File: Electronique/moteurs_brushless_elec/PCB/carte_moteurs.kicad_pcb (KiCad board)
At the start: 2 copper layers, 154 x 65 mm, 86 parts, among them J1 CONN_SERIAL, J2 swdio, J3 FAN, K1 Maxon-200142, K2 Maxon-200142, P1 CONN_I2C, P2 CONN_FREE, P3 CONN_CAN, P4 encoder_2, P5 encoder_1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

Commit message: trous et dim o
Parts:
- C2, Cboot2, Cen2, Coff2, Cp2, Cpul2, D10, D6, R8, R9, Rdd2, Ren2, Roff2, Rp2, Rpul2, U5, U6: moved to B.Cu
- moved Y1 319.6 mm to (242.0, 144.0)
- moved C3 312.7 mm to (229.2, 145.2)
- moved C4 312.7 mm to (236.2, 156.2)
- moved R14 298.7 mm to (226.0, 154.0), turned to 0 degrees
- moved P1 268.7 mm to (176.0, 123.0)
- moved J2 268.7 mm to (174.0, 146.0), turned to 270 degrees
- moved JP1 260.3 mm to (176.1, 89.8)
- moved R5 241.9 mm to (162.2, 103.1)
- moved P3 241.0 mm to (176.0, 129.5), turned to 90 degrees
- moved U3 240.1 mm to (152.7, 159.8), turned to 270 degrees
- moved D5 239.5 mm to (161.0, 139.0)
- moved R6 238.4 mm to (159.0, 131.0), turned to 0 degrees
- moved J1 237.5 mm to (176.0, 134.0), turned to 270 degrees
- moved P2 237.2 mm to (176.0, 113.5)
- moved C5 237.1 mm to (152.0, 113.0), turned to 90 degrees
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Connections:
- J3 pad 1: VCC -> VDD
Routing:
- net GND: track 0.00 -> 222.6 mm, vias 0 -> 4
- net VDD: track 0.00 -> 53.3 mm, vias 0 -> 1
- net VCC: track 0.00 -> 49.8 mm, vias 0 -> 2
- net /motor_part/DIAG_2: track 0.00 -> 44.6 mm, vias 0 -> 2
- net Net-(K1-Pad5): track 0.00 -> 37.6 mm, vias 0 -> 1
- net Net-(K1-Pad1): track 0.00 -> 30.0 mm, vias 0 -> 1
- net Net-(F2-Pad2): track 0.00 -> 28.9 mm
- net Net-(F1-Pad2): track 0.00 -> 28.9 mm
- net Net-(K2-Pad1): track 0.00 -> 28.6 mm, vias 0 -> 1
- net Net-(K2-Pad9): track 0.00 -> 26.1 mm, vias 0 -> 1
- net Net-(K2-Pad5): track 0.00 -> 25.9 mm, vias 0 -> 1
- net Net-(K2-Pad3): track 0.00 -> 25.5 mm, vias 0 -> 1
- net Net-(Rsense2-Pad1): track 0.00 -> 24.3 mm
- net Net-(K1-Pad3): track 0.00 -> 21.9 mm, vias 0 -> 1
- net /motor_part/Vref2: track 0.00 -> 20.6 mm, vias 0 -> 2
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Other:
- net class Default: trace_width 0.508 -> 0.4

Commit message: trous et dim
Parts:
- C1, C5, Cboot1, Cen1, Coff1, Cp1, Cpul1, R11, R12, Rdd1, Ren1, Roff1, Rp1, Rpul1: moved to B.Cu
- moved R8 89.3 mm to (29.7, 117.7)
- moved U5 89.3 mm to (38.9, 117.7)
- moved R9 89.2 mm to (29.7, 125.3)
- moved C8 87.6 mm to (48.7, 118.8), turned to 90 degrees
- moved D8 83.8 mm to (41.4, 133.1)
- moved R10 83.8 mm to (34.5, 131.1)
- moved Cen1 77.5 mm to (122.7, 128.7), turned to 270 degrees
- moved Ren1 77.1 mm to (120.3, 128.7), turned to 270 degrees
- moved Rpul1 68.7 mm to (139.8, 129.2), turned to 270 degrees
- moved Cpul1 64.7 mm to (142.2, 129.2), turned to 270 degrees
- moved Rdd1 59.7 mm to (134.4, 129.1), turned to 270 degrees
- moved Roff1 55.8 mm to (127.2, 128.9), turned to 270 degrees
- moved R2 51.8 mm to (144.3, 110.7), turned to 180 degrees
- moved Coff1 50.9 mm to (129.7, 128.8), turned to 270 degrees
- moved U3 48.8 mm to (158.5, 111.4)
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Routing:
- net GND: track 222.6 -> 706.0 mm, vias 4 -> 20
- net +3V3: track 0.00 -> 264.5 mm, vias 0 -> 6
- net +5V: track 18.4 -> 229.7 mm, vias 0 -> 7
- net VCC: track 49.8 -> 232.7 mm, vias 2 -> 3
- net /motor_part/BRAKE_2: track 0.00 -> 179.7 mm, vias 0 -> 4
- net /motor_part/DIR_2: track 0.00 -> 159.1 mm, vias 0 -> 2
- net /motor_part/TACHO_2: track 17.8 -> 161.3 mm, vias 1 -> 8
- net /motor_part/DIAG_2: track 44.6 -> 176.8 mm, vias 2 -> 5
- net /motor_part/EN_2: track 0.00 -> 120.5 mm, vias 0 -> 1
- net /uC/nrst: track 0.00 -> 88.7 mm, vias 0 -> 3
- net /motor_part/DIAG_1: track 0.00 -> 72.5 mm, vias 0 -> 4
- net /uC/RX: track 0.00 -> 58.3 mm, vias 0 -> 1
- net /encodeurs/Ch_A1: track 0.00 -> 56.8 mm, vias 0 -> 3
- net VDD: track 53.3 -> 108.7 mm
- net /motor_part/TACHO_1: track 0.00 -> 53.8 mm, vias 0 -> 4
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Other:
- net class Default: trace_width 0.4 -> 1.2

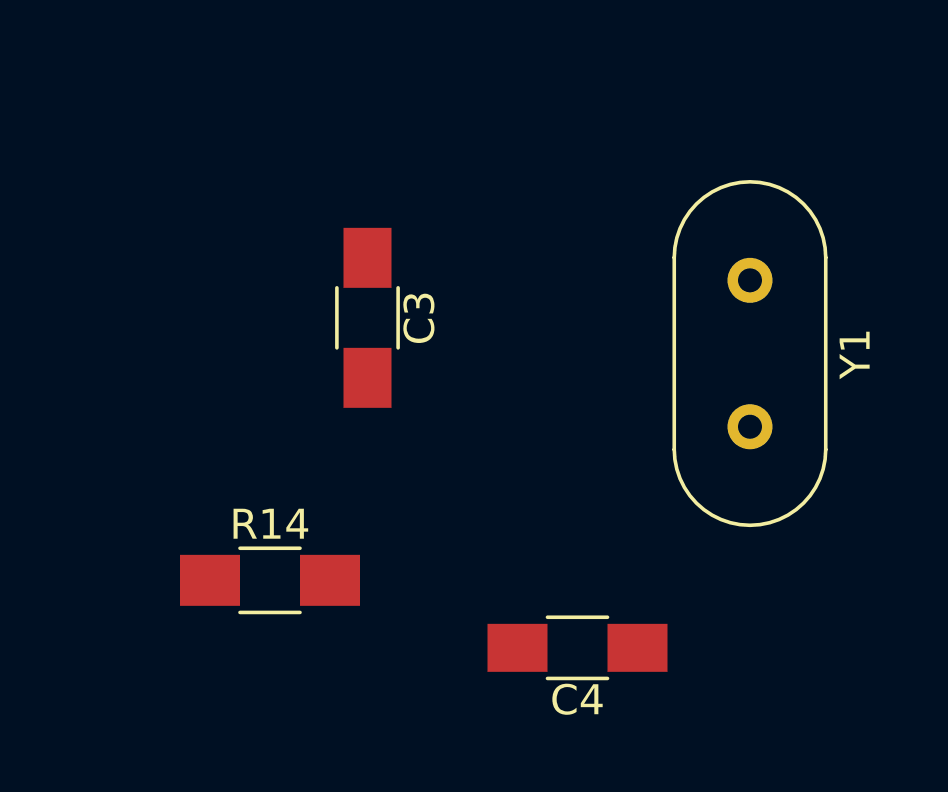
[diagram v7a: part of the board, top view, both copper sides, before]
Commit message: pas de place pour le quartz
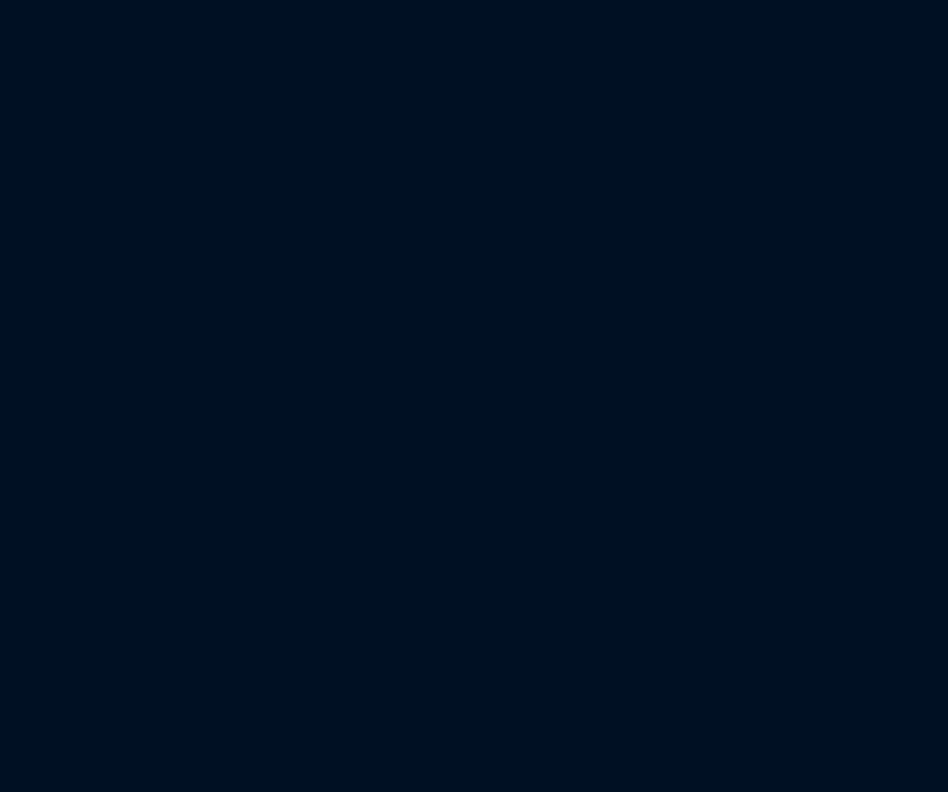
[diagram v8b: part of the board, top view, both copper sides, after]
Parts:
- removed C3, C4: 10nC, Capacitors_SMD:C_1206_HandSoldering
- removed R14: R, Resistors_SMD:R_1206_HandSoldering
- removed Y1: Crystal_8MHz, Crystals:Crystal_HC49-4H_Vertical
